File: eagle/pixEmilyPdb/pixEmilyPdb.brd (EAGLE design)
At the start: 35.2 x 14 mm, 8 parts

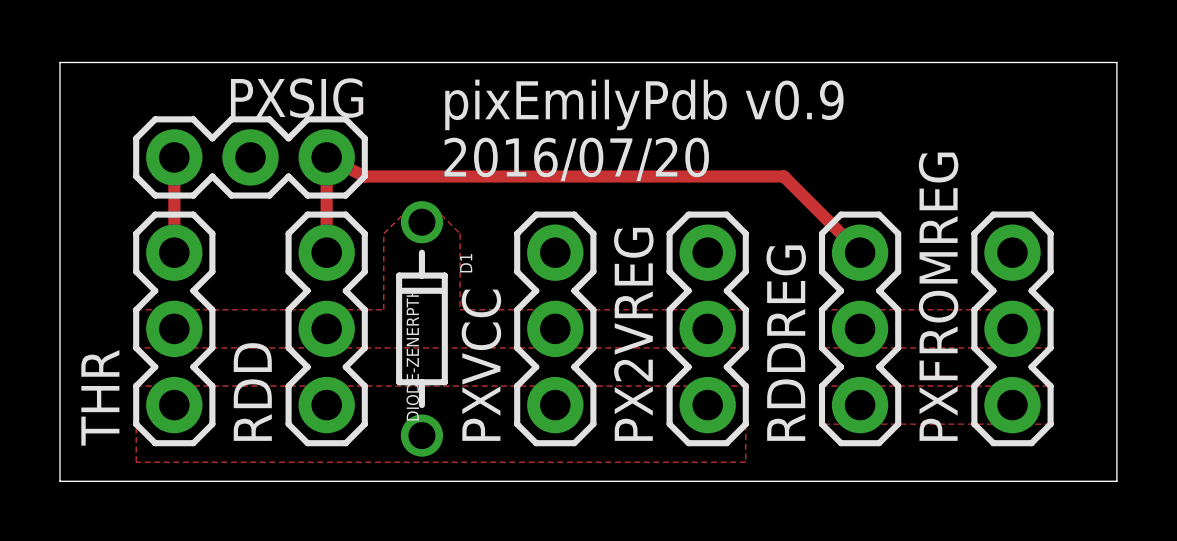
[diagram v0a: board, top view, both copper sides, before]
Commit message: Updated PBD with mounting holes & misc fixes
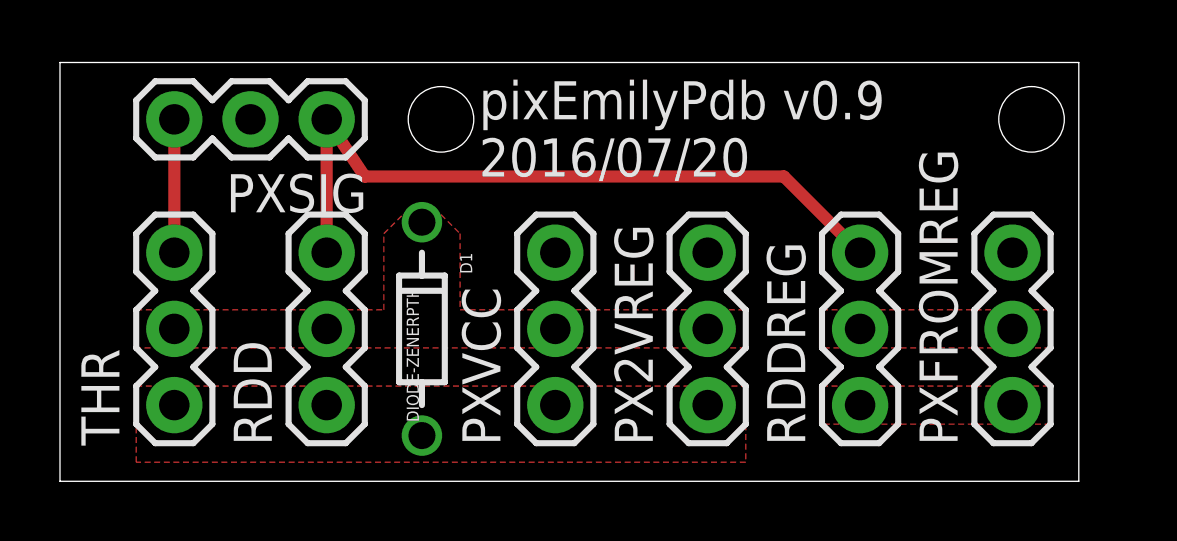
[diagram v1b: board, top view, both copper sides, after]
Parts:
- moved PXSIG 1.27 mm to (8.89, 12.1)
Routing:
- net RDDSIG: track 22.2 -> 24.3 mm
- net THRSIG: track 3.17 -> 4.44 mm
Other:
- board size 35.2 x 14 mm -> 34 x 14 mm
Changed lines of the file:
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@@
 <layer number="43" name="vRestrict" color="2" fill="10" visible="yes" active="yes"/>
 <layer number="44" name="Drills" color="7" fill="1" visible="no" active="yes"/>
-<layer number="45" name="Holes" color="7" fill="1" visible="no" active="yes"/>
+<layer number="45" name="Holes" color="7" fill="1" visible="yes" active="yes"/>
 <layer number="46" name="Milling" color="3" fill="1" visible="no" active="yes"/>
 <layer number="47" name="Measures" color="7" fill="1" visible="no" active="yes"/>
@@
 <board>
 <plain>
-<wire x1="0" y1="0" x2="35.23" y2="0" width="0" layer="20"/>
-<wire x1="35.23" y1="0" x2="35.23" y2="13.96" width="0" layer="20"/>
-<wire x1="35.23" y1="13.96" x2="0" y2="13.96" width="0" layer="20"/>
+<wire x1="0" y1="0" x2="33.96" y2="0" width="0" layer="20"/>
+<wire x1="33.96" y1="0" x2="33.96" y2="13.96" width="0" layer="20"/>
+<wire x1="33.96" y1="13.96" x2="0" y2="13.96" width="0" layer="20"/>
 <wire x1="0" y1="13.96" x2="0" y2="0" width="0" layer="20"/>
-<text x="12.7" y="10.16" size="1.27" layer="25" font="vector">pixEmilyPdb v0.9
+<text x="13.97" y="10.16" size="1.27" layer="25" font="vector">pixEmilyPdb v0.9
 2016/07/20</text>
+<hole x="32.385" y="12.065" drill="2.1844"/>
+<hole x="12.7" y="12.065" drill="2.1844"/>
 </plain>
 <attributes>
@@
 </class>
 </classes>
-<designrules name="default">
+<designrules name="LaenPCBOrder">
 <description language="de">&lt;b&gt;EAGLE Design Rules&lt;/b&gt;
 &lt;p&gt;
@@
 Einstellungen hier und speichern die Design Rules unter
 einem neuen Namen ab.</description>
-<description language="en">&lt;b&gt;EAGLE Design Rules&lt;/b&gt;
+<description language="en">&lt;b&gt;Laen's PCB Order Design Rules&lt;/b&gt;
 &lt;p&gt;
-The default Design Rules have been set to cover
-a wide range of applications. Your particular design
-may have different requirements, so please make the
-necessary adjustments and save your customized
-design rules under a new name.</description>
+Please make sure your boards conform to these design rules.</description>
 <param name="layerSetup" value="(1*16)"/>
-<param name="mtCopper" value="0.035mm 0.035mm 0.035mm 0.035mm 0.035mm 0.035mm 0.035mm 0.035mm 0.035mm 0.035mm 0.035mm 0.035mm 0.035mm 0.035mm 0.035mm 0.035mm"/>
-<param name="mtIsolate" value="1.5mm 0.15mm 0.2mm 0.15mm 0.2mm 0.15mm 0.2mm 0.15mm 0.2mm 0.15mm 0.2mm 0.15mm 0.2mm 0.15mm 0.2mm"/>
-<param name="mdWireWire" value="8mil"/>
-<param name="mdWirePad" value="8mil"/>
-<param name="mdWireVia" value="8mil"/>
-<param name="mdPadPad" value="8mil"/>
-<param name="mdPadVia" value="8mil"/>
-<param name="mdViaVia" value="8mil"/>
-<param name="mdSmdPad" value="8mil"/>
-<param name="mdSmdVia" value="8mil"/>
-<param name="mdSmdSmd" value="8mil"/>
+<param name="mtCopper" value="0.0356mm 0.0356mm 0.0356mm 0.0356mm 0.0356mm 0.0356mm 0.0356mm 0.0356mm 0.0356mm 0.0356mm 0.0356mm 0.0356mm 0.0356mm 0.0356mm 0.0356mm 0.0356mm"/>
+<param name="mtIsolate" value="1.5011mm 0.1499mm 0.2007mm 0.1499mm 0.2007mm 0.1499mm 0.2007mm 0.1499mm 0.2007mm 0.1499mm 0.2007mm 0.1499mm 0.2007mm 0.1499mm 0.2007mm"/>
+<param name="mdWireWire" value="6mil"/>
+<param name="mdWirePad" value="6mil"/>
+<param name="mdWireVia" value="6mil"/>
+<param name="mdPadPad" value="6mil"/>
+<param name="mdPadVia" value="6mil"/>
+<param name="mdViaVia" value="6mil"/>
+<param name="mdSmdPad" value="6mil"/>
+<param name="mdSmdVia" value="6mil"/>
+<param name="mdSmdSmd" value="6mil"/>
 <param name="mdViaViaSameLayer" value="8mil"/>
 <param name="mnLayersViaInSmd" value="2"/>
-<param name="mdCopperDimension" value="40mil"/>
-<param name="mdDrill" value="8mil"/>
+<param name="mdCopperDimension" value="15mil"/>
+<param name="mdDrill" value="6mil"/>
 <param name="mdSmdStop" value="0mil"/>
-<param name="msWidth" value="10mil"/>
-<param name="msDrill" value="24mil"/>
-<param name="msMicroVia" value="9.99mm"/>
+<param name="msWidth" value="6mil"/>
+<param name="msDrill" value="13mil"/>
+<param name="msMicroVia" value="13mil"/>
 <param name="msBlindViaRatio" value="0.5"/>
 <param name="rvPadTop" value="0.25"/>
@@
 <param name="rvMicroViaOuter" value="0.25"/>
 <param name="rvMicroViaInner" value="0.25"/>
-<param name="rlMinPadTop" value="10mil"/>
+<param name="rlMinPadTop" value="7mil"/>
 <param name="rlMaxPadTop" value="20mil"/>
-<param name="rlMinPadInner" value="10mil"/>
+<param name="rlMinPadInner" value="7mil"/>
 <param name="rlMaxPadInner" value="20mil"/>
-<param name="rlMinPadBottom" value="10mil"/>
+<param name="rlMinPadBottom" value="7mil"/>
 <param name="rlMaxPadBottom" value="20mil"/>
-<param name="rlMinViaOuter" value="8mil"/>
+<param name="rlMinViaOuter" value="7mil"/>
 <param name="rlMaxViaOuter" value="20mil"/>
-<param name="rlMinViaInner" value="8mil"/>
+<param name="rlMinViaInner" value="7mil"/>
 <param name="rlMaxViaInner" value="20mil"/>
 <param name="rlMinMicroViaOuter" value="4mil"/>
@@
 <param name="mvStopFrame" value="1"/>
 <param name="mvCreamFrame" value="0"/>
-<param name="mlMinStopFrame" value="4mil"/>
-<param name="mlMaxStopFrame" value="4mil"/>
+<param name="mlMinStopFrame" value="3mil"/>
+<param name="mlMaxStopFrame" value="3mil"/>
 <param name="mlMinCreamFrame" value="0mil"/>
 <param name="mlMaxCreamFrame" value="0mil"/>
@@
 <elements>
 <element name="D1" library="SparkFun-DiscreteSemi" package="DIODE-ZENER" value="DIODE-ZENERPTH" x="12.065" y="5.08" rot="R270"/>
-<element name="PXSIG" library="SparkFun-Connectors" package="1X03" value="" x="8.89" y="10.795" smashed="yes" rot="R180">
-<attribute name="NAME" x="10.2362" y="13.4112" size="1.27" layer="25" font="vector" ratio="10" rot="R180"/>
-<attribute name="VALUE" x="10.16" y="13.97" size="1.27" layer="27" rot="R180"/>
+<element name="PXSIG" library="SparkFun-Connectors" package="1X03" value="" x="8.89" y="12.065" smashed="yes" rot="R180">
+<attribute name="NAME" x="10.2362" y="10.2362" size="1.27" layer="25" font="vector" ratio="10" rot="R180"/>
+<attribute name="VALUE" x="10.16" y="15.24" size="1.27" layer="27" rot="R180"/>
 </element>
 <element name="PXVCC" library="SparkFun-Connectors" package="1X03" value="" x="16.51" y="2.54" smashed="yes" rot="R90">
@@
 <contactref element="RDD" pad="3"/>
 <contactref element="RDDREG" pad="3"/>
-<wire x1="8.89" y1="7.62" x2="8.89" y2="10.795" width="0.4064" layer="1"/>
+<wire x1="8.89" y1="7.62" x2="8.89" y2="12.065" width="0.4064" layer="1"/>
 <wire x1="10.16" y1="10.16" x2="24.13" y2="10.16" width="0.4064" layer="1"/>
 <wire x1="24.13" y1="10.16" x2="26.67" y2="7.62" width="0.4064" layer="1"/>
-<wire x1="10.16" y1="10.16" x2="8.89" y2="10.795" width="0.4064" layer="1"/>
+<wire x1="10.16" y1="10.16" x2="8.89" y2="12.065" width="0.4064" layer="1"/>
 </signal>
 <signal name="THRSIG">
 <contactref element="PXSIG" pad="3"/>
 <contactref element="THR" pad="3"/>
-<wire x1="3.81" y1="7.62" x2="3.81" y2="10.795" width="0.4064" layer="1"/>
+<wire x1="3.81" y1="7.62" x2="3.81" y2="12.065" width="0.4064" layer="1"/>
 </signal>
 <signal name="VCCEXT">
